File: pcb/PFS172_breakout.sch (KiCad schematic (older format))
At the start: 3 parts, among them J2 Conn_01x04_Male, J3 Conn_01x04_Male, U1 PFS173-S08

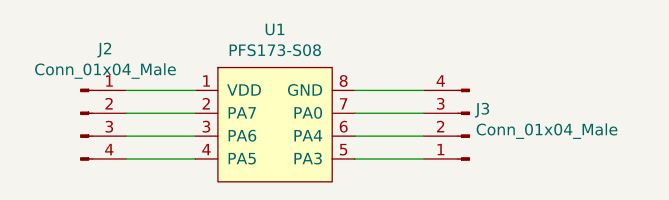
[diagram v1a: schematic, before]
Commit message: Added buzzer
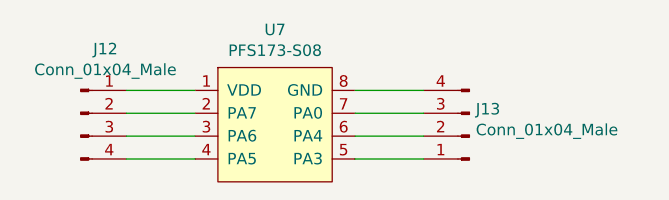
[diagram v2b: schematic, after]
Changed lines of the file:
@@
 $Descr A4 11693 8268
 encoding utf-8
-Sheet 3 10
+Sheet 3 12
 Title ""
 Date ""
@@
 AR Path="/60318BF9/602FDA9E" Ref="U6"  Part="1"
 AR Path="/60318BFB/602FDA9E" Ref="U7"  Part="1"
-F 0 "U1" H 5200 3665 50  0000 C CNN
+F 0 "U7" H 5200 3665 50  0000 C CNN
 F 1 "PFS173-S08" H 5200 3574 50  0000 C CNN
 F 2 "Package_SO:SOP-8_3.9x4.9mm_P1.27mm" H 5200 2850 50  0001 C CNN
@@
 AR Path="/60318BF9/60300751" Ref="J11"  Part="1"
 AR Path="/60318BFB/60300751" Ref="J13"  Part="1"
-F 0 "J3" H 6022 3182 50  0000 R CNN
+F 0 "J13" H 6022 3182 50  0000 R CNN
 F 1 "Conn_01x04_Male" H 6022 3273 50  0000 R CNN
 F 2 "Connector_PinHeader_2.54mm:PinHeader_1x04_P2.54mm_Vertical" H 6050 3300 50  0001 C CNN
@@
 AR Path="/60318BF9/6030287E" Ref="J10"  Part="1"
 AR Path="/60318BFB/6030287E" Ref="J12"  Part="1"
-F 0 "J2" H 4458 3481 50  0000 C CNN
+F 0 "J12" H 4458 3481 50  0000 C CNN
 F 1 "Conn_01x04_Male" H 4458 3390 50  0000 C CNN
 F 2 "Connector_PinHeader_2.54mm:PinHeader_1x04_P2.54mm_Vertical" H 4350 3200 50  0001 C CNN
